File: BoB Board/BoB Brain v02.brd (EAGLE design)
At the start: 50 x 50 mm, 41 parts, among them CN1 USB_CON, Q1 MOSFET-NCHANNELAO3404A, Q9 MOSFET-NCHANNELAO3404A, U1 ATMEGA328P_TQFP, U2 CH340G, U3 +12v, U4 V_REG_317SMD, Y1 16MHZ

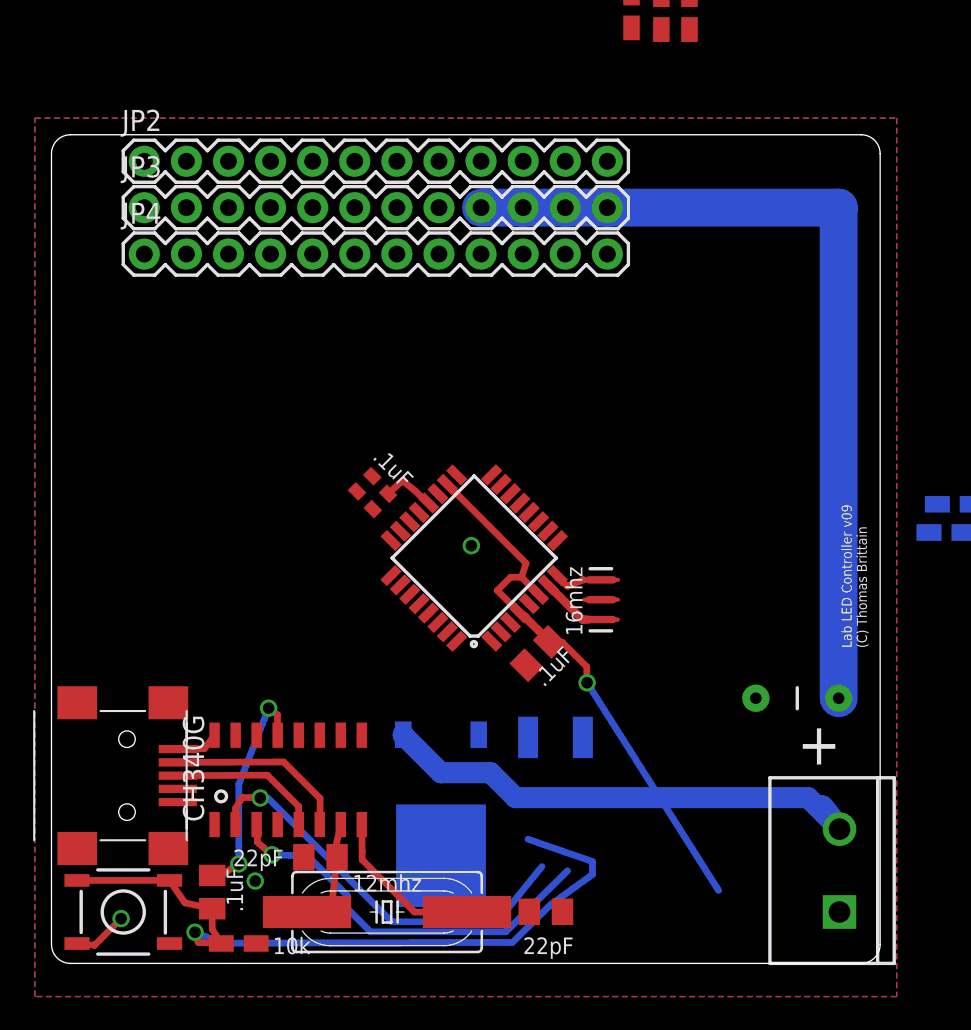
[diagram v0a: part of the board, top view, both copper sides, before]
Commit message: Added servo / digital power rails
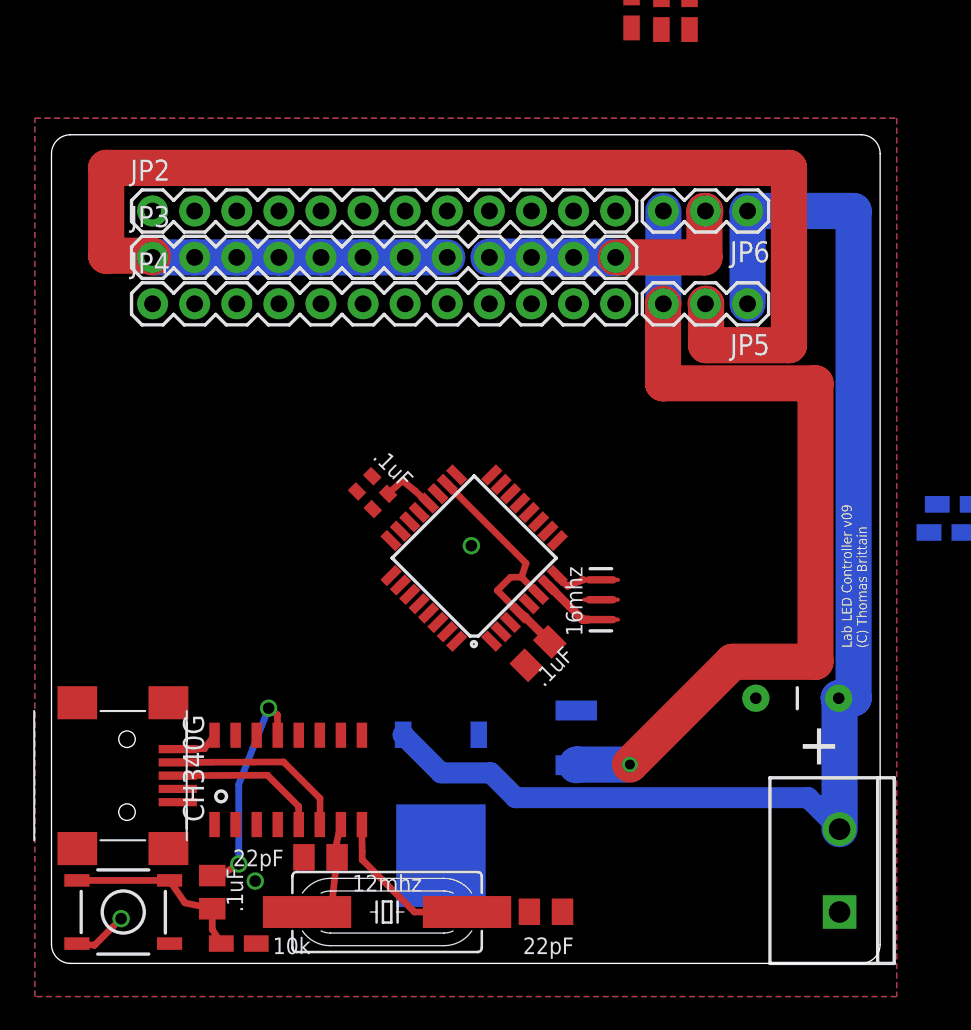
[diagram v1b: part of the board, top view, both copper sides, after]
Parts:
- added JP5, JP6: JUMPER-3PTH, SparkFun-Retired:1X03
- moved JP2 3.04 mm to (6.10, 45.4)
- moved JP3 3.04 mm to (6.10, 42.6)
- moved JP4 3.04 mm to (6.10, 39.8)
- moved C2 1.26 mm to (31.7, 13.6), turned to 270 degrees
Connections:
- new net N$10: JP4.11
- new net N$16: JP4.10
- new net N$17: JP4.9
- new net N$18: JP4.8
- new net N$19: JP4.7
- new net N$20: JP4.6
- new net N$21: JP4.5
- new net N$22: JP4.4
- new net N$23: JP4.3
- new net N$24: JP4.2
- new net N$25: JP4.1
- new net N$7: JP4.12
- new net PIN_PWR: JP3.1, JP3.2, JP3.3, JP3.4, JP3.5, JP3.6, JP3.7, JP3.8, JP5.2
- new net RAW: C1.1, JP1.2, JP5.1, JP6.1, U3.1
- net 6V: now also JP6.2; no longer C1.1, JP1.2, U3.1
- net GND: now also JP2.1, JP2.10, JP2.11, JP2.12, JP2.2, JP2.3, JP2.4, JP2.5, JP2.6, JP2.7, JP2.8, JP2.9
- net VCC: now also JP5.3, JP6.3; no longer JP3.1, JP3.2, JP3.3, JP3.4, JP3.5, JP3.6, JP3.7, JP3.8
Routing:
- net PIN_PWR: track 0.00 -> 85.4 mm
- net RAW: track 0.00 -> 80.7 mm
- net 6V: track 81.6 -> 15.8 mm
- net VCC: track 36.7 -> 71.5 mm
- net N$13: track 43.8 -> 11.3 mm, vias 1 -> 0
- net U2_TX: track 24.5 -> 0.00 mm, vias 1 -> 0
- net U2_RX: track 23.9 -> 0.00 mm, vias 1 -> 0
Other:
- board text removed: "3.3k"

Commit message: Working on BoB Board
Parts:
- removed C6, C7: 22pF, resistor:C0805K
- removed C9: 0.1uF, resistor:C0805K
- removed CN1: USB_CON, adafruit:USB-MINIB
- removed R10, R16: 3.3k, resistor:R0805W
- removed R15: 10k, resistor:R0805W
- removed R23: 20k, resistor:R0805W
- removed RESONATOR: 16mhz, crystal:HC49UP
- removed U2: CH340G, usb-serial:SOIC16
- added R1, R2: 1K, resistor:R0805W
- U$1: value ESP8266-07 -> HM-11; device lio:ESP-07 -> HM-11-ladvien:HM-11
- moved U$1 99.9 mm to (-24.3, -2.10), flipped to the top, turned to 0 degrees
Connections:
- removed net 12: R15.2, R23.2, U1.16
- removed net D+: CN1.D+, U2.5
- removed net D-: CN1.D-, U2.6
- removed net ESP-RX: Q9.3, R19.1, U1.11
- removed net ESP-TX: Q1.3, R20.1, U1.10
- removed net X0: C7.1, RESONATOR.2, U2.8
- removed net X1: C6.1, RESONATOR.1, U2.7
- new net ATMEGA-RESET: R2.1, U$1.14
- new net HM-RESET: R1.1, U1.32
- new net N$26: U1.28
- new net N$27: U1.19
- new net N$28: U1.22
- new net N$29: U1.1
- new net N$30: U1.2
- new net N$31: U1.10
- new net N$32: U1.11
- new net N$33: U1.12
- new net RESET: C5.2, R1.2, R14.1, R2.2, S1.3, S1.4, U$1.11, U1.29
- net 3.35V: now also U$1.9; no longer C9.1, R10.1, U$1.CH_PD, U$1.VCC
- net DTR: no longer U2.13
- net GND: now also U$1.12; no longer C6.2, C7.2, C9.2, CN1.GND, R16.1, R23.1, U$1.GND, U2.1
- net N$12: now also U$1.2; no longer U$1.TXD
- net N$13: now also U1.27; no longer C5.2, R14.1, S1.3, S1.4, U1.29
- net N$15: now also U$1.4; no longer U$1.RXD
- net N$3: now also U1.16; no longer R15.1, U$1.REST
- net N$4: now also U1.23; no longer R10.2, U$1.GPIO2
- net N$5: now also U1.26; no longer R16.2, U$1.GPIO15
- net U2_RX: now also Q1.3, R20.1; no longer U2.3
- net U2_TX: now also Q9.3, R19.1; no longer U2.2
- net VCC: no longer CN1.VBUS, U2.16
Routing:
- net RESET: track 0.00 -> 11.3 mm
- net N$13: track 11.3 -> 0.00 mm
- net D-: track 11.1 -> 0.00 mm
- net X0: track 9.76 -> 0.00 mm
- net D+: track 9.17 -> 0.00 mm
- net X1: track 8.18 -> 0.00 mm
- net VCC: track 71.5 -> 68.8 mm
- net DTR: track 13.8 -> 12.6 mm

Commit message: Working on BoB board
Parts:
- moved U1 0.56 mm to (25.1, 24.8), turned to 45 degrees
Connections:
- net 10 renamed 10~
- net 11 renamed 11~
- net 5 renamed 5~
- net 9 renamed 9~
- net N$13 renamed A4-SDA
- net N$26 renamed A5-SCL
- net N$27 renamed ADC6
- net N$28 renamed ADC7
- net N$29 renamed 3~
- net N$3 renamed 12
- net N$30 renamed 4
- net N$31 renamed 6~
- net N$32 renamed 7
- net N$33 renamed 8
- net N$4 renamed A0
- net N$5 renamed A3
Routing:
- net VCC: track 68.8 -> 82.2 mm
- net N$2: track 4.08 -> 16.7 mm
- net N$11: track 2.01 -> 9.28 mm
- net RESET: track 11.3 -> 17.7 mm
- net N$1: track 3.26 -> 8.89 mm
